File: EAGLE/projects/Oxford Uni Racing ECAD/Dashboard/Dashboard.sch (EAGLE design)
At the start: 19 parts, among them J1 T821108A1S100CEU, J2 CAN_OUT, J3 PWR_CAN, J4 DISPL, J5 BUTTONS, K1 EC2-12NU, K2 EC2-12NU, X2 D-SUB9-H2M09ST

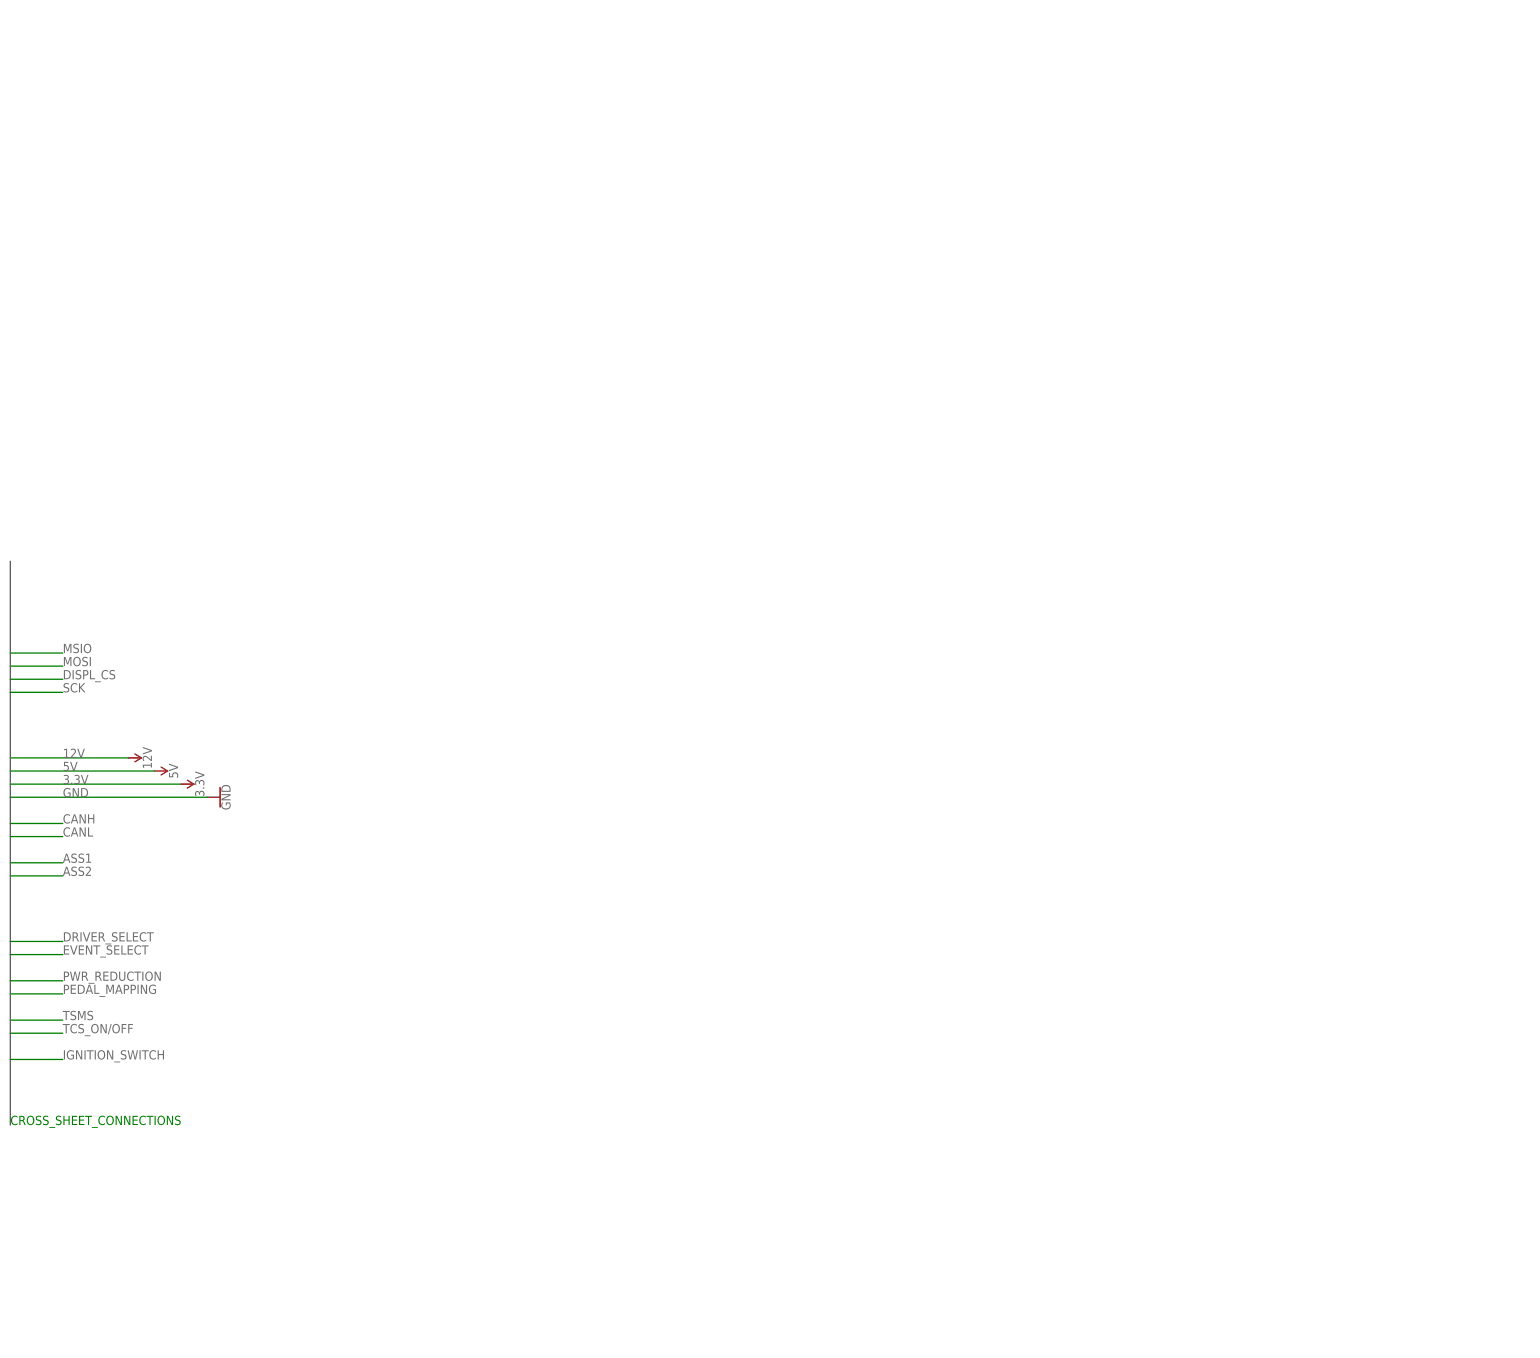
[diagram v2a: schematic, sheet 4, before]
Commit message: added microcontroller to dashboard
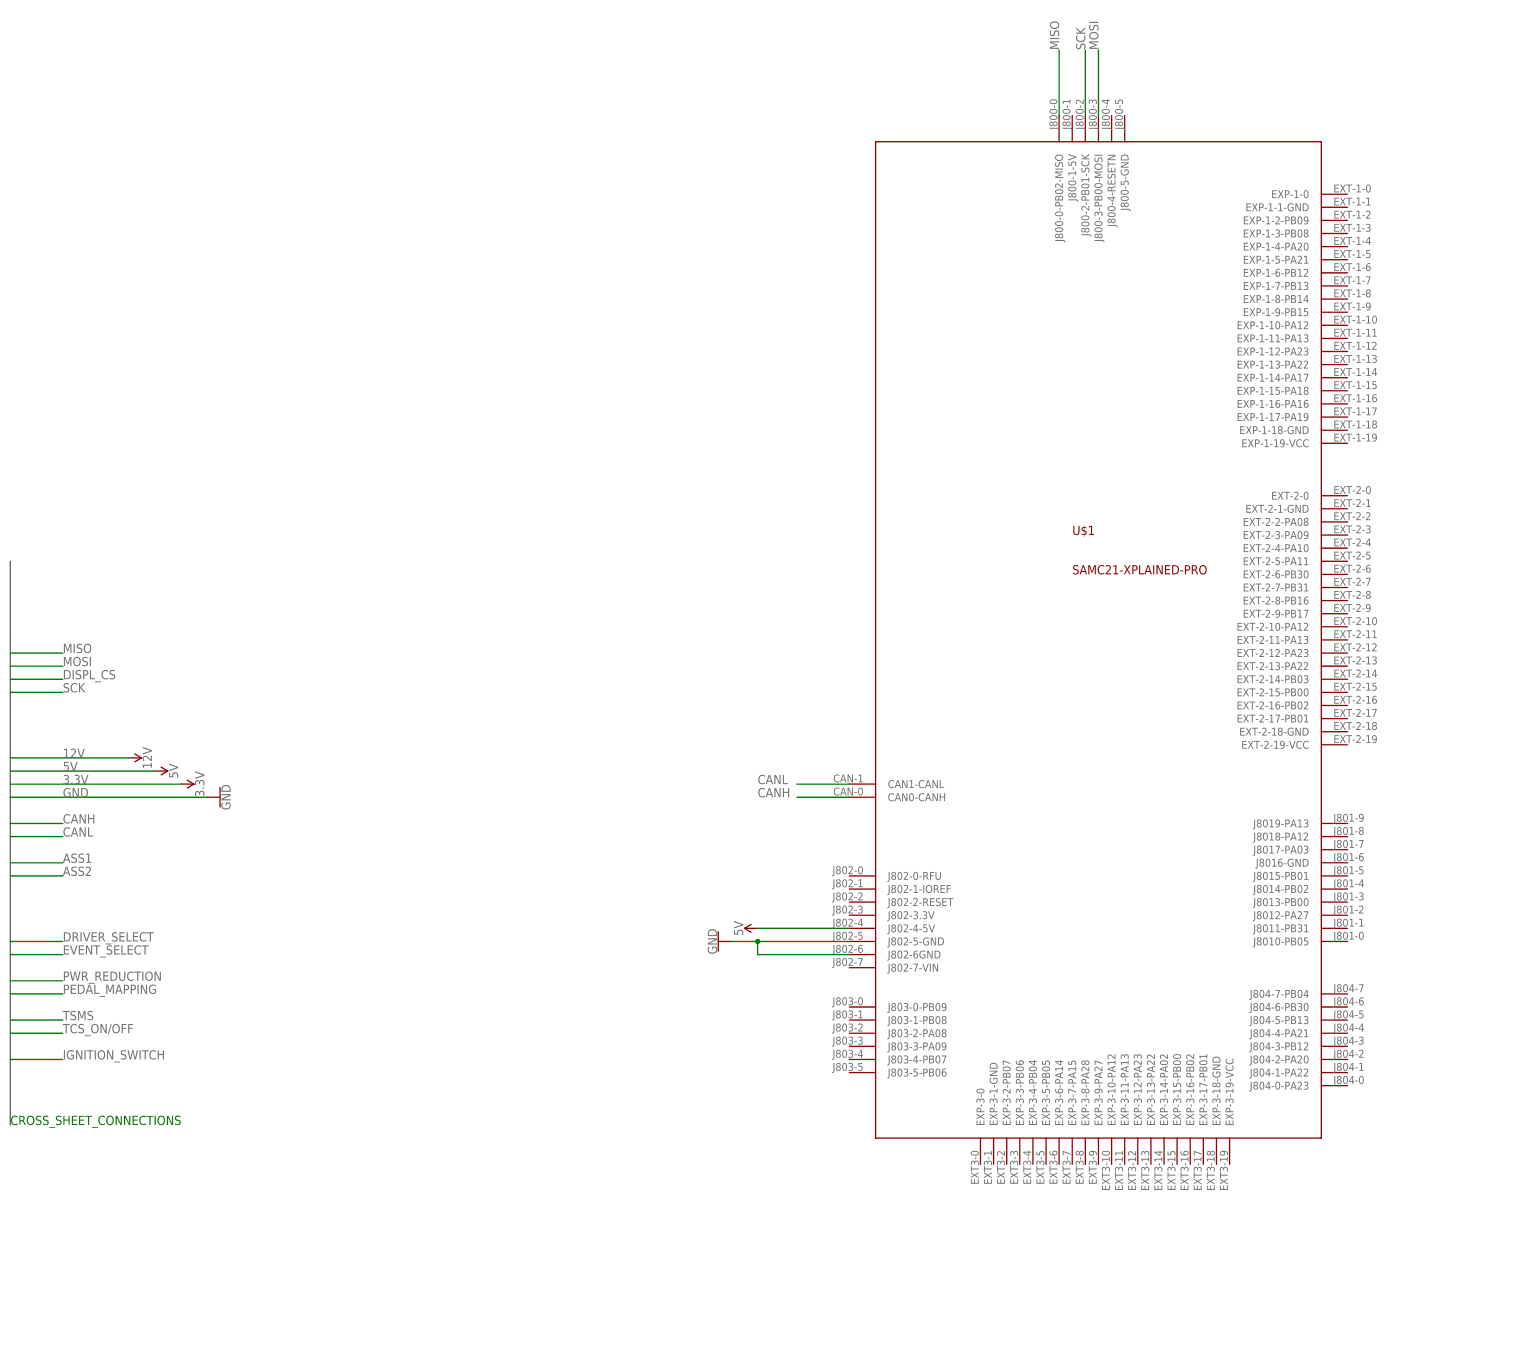
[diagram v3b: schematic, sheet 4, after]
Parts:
- added U$1: SAMC21-XPLAINED-PRO, Oxford Uni Racing Custom Blueprints:SAMC21-XPLAINED-PRO
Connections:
- removed net DISPL_SCL: J4.7
- removed net DISPL_SDA: J4.5
- new net DISPL_CS: J4.8
- new net MISO: J4.5, U$1.J800-0-PB02-MISO
- new net MOSI: J4.6, U$1.J800-3-PB00-MOSI
- new net SCK: J4.7, U$1.J800-2-PB01-SCK
- net 5V: now also U$1.J802-4-5V
- net CANH: now also U$1.CAN0-CANH
- net CANL: now also U$1.CAN1-CANL
- net GND: now also U$1.J802-5-GND, U$1.J802-6GND
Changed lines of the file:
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@@
 <part name="SUPPLY31" library="SparkFun-PowerSymbols" library_urn="urn:adsk.eagle:library:530" deviceset="3.3V" device=""/>
 <part name="GND8" library="SparkFun-PowerSymbols" library_urn="urn:adsk.eagle:library:530" deviceset="GND" device=""/>
+<part name="U$1" library="Oxford Uni Racing Custom Blueprints" deviceset="SAMC21-XPLAINED-PRO" device=""/>
+<part name="SUPPLY32" library="SparkFun-PowerSymbols" library_urn="urn:adsk.eagle:library:530" deviceset="5V" device=""/>
+<part name="GND21" library="SparkFun-PowerSymbols" library_urn="urn:adsk.eagle:library:530" deviceset="GND" device=""/>
 </parts>
 <sheets>
@@
 </segment>
 </net>
-<net name="MSIO" class="0">
+<net name="MISO" class="0">
 <segment>
 <label x="10.16" y="91.44" size="1.778" layer="95"/>
@@
 </segment>
 </net>
-<net name="MSIO" class="0">
+<net name="MISO" class="0">
 <segment>
 <label x="10.16" y="91.44" size="1.778" layer="95"/>
@@
 </segment>
 </net>
-<net name="MSIO" class="0">
+<net name="MISO" class="0">
 <segment>
 <label x="10.16" y="91.44" size="1.778" layer="95"/>
@@
 <attribute name="VALUE" x="40.894" y="63.5" size="1.778" layer="96" rot="R90" align="top-center"/>
 </instance>
+<instance part="U$1" gate="G$1" x="167.64" y="-2.54" smashed="yes">
+<attribute name="NAME" x="205.74" y="114.3" size="1.778" layer="94"/>
+<attribute name="VALUE" x="205.74" y="106.68" size="1.778" layer="94"/>
+</instance>
+<instance part="SUPPLY32" gate="G$1" x="144.78" y="38.1" smashed="yes" rot="R90">
+<attribute name="VALUE" x="141.986" y="38.1" size="1.778" layer="96" rot="R90" align="bottom-center"/>
+</instance>
+<instance part="GND21" gate="1" x="137.16" y="35.56" smashed="yes" rot="R270">
+<attribute name="VALUE" x="136.906" y="35.56" size="1.778" layer="96" rot="R270" align="top-center"/>
+</instance>
 </instances>
 <busses>
@@
 <wire x1="27.94" y1="68.58" x2="0" y2="68.58" width="0.1524" layer="91"/>
 </segment>
+<segment>
+<pinref part="U$1" gate="G$1" pin="J802-4-5V"/>
+<wire x1="162.56" y1="38.1" x2="144.78" y2="38.1" width="0.1524" layer="91"/>
+<pinref part="SUPPLY32" gate="G$1" pin="5V"/>
+</segment>
 </net>
 <net name="3.3V" class="0">
@@
 <wire x1="38.1" y1="63.5" x2="0" y2="63.5" width="0.1524" layer="91"/>
 </segment>
+<segment>
+<pinref part="U$1" gate="G$1" pin="J802-5-GND"/>
+<wire x1="162.56" y1="35.56" x2="144.78" y2="35.56" width="0.1524" layer="91"/>
+<pinref part="GND21" gate="1" pin="GND"/>
+<pinref part="U$1" gate="G$1" pin="J802-6GND"/>
+<wire x1="144.78" y1="35.56" x2="139.7" y2="35.56" width="0.1524" layer="91"/>
+<wire x1="162.56" y1="33.02" x2="144.78" y2="33.02" width="0.1524" layer="91"/>
+<wire x1="144.78" y1="33.02" x2="144.78" y2="35.56" width="0.1524" layer="91"/>
+<junction x="144.78" y="35.56"/>
+</segment>
 </net>
 <net name="CANH" class="0">
@@
 <wire x1="10.16" y1="58.42" x2="0" y2="58.42" width="0.1524" layer="91"/>
 </segment>
+<segment>
+<pinref part="U$1" gate="G$1" pin="CAN0-CANH"/>
+<wire x1="162.56" y1="63.5" x2="152.4" y2="63.5" width="0.1524" layer="91"/>
+<label x="144.78" y="63.5" size="1.778" layer="95"/>
+</segment>
 </net>
 <net name="CANL" class="0">
@@
 <wire x1="10.16" y1="55.88" x2="0" y2="55.88" width="0.1524" layer="91"/>
 </segment>
+<segment>
+<pinref part="U$1" gate="G$1" pin="CAN1-CANL"/>
+<wire x1="162.56" y1="66.04" x2="152.4" y2="66.04" width="0.1524" layer="91"/>
+<label x="144.78" y="66.04" size="1.778" layer="95"/>
+</segment>
 </net>
 <net name="ASS1" class="0">
@@
 <wire x1="10.16" y1="83.82" x2="0" y2="83.82" width="0.1524" layer="91"/>
 </segment>
+<segment>
+<pinref part="U$1" gate="G$1" pin="J800-2-PB01-SCK"/>
+<wire x1="208.28" y1="195.58" x2="208.28" y2="208.28" width="0.1524" layer="91"/>
+<label x="208.28" y="208.28" size="1.778" layer="95" rot="R90"/>
+</segment>
 </net>
 <net name="DISPL_CS" class="0">
@@
 <wire x1="10.16" y1="88.9" x2="0" y2="88.9" width="0.1524" layer="91"/>
 </segment>
-</net>
-<net name="MSIO" class="0">
+<segment>
+<pinref part="U$1" gate="G$1" pin="J800-3-PB00-MOSI"/>
+<wire x1="210.82" y1="195.58" x2="210.82" y2="208.28" width="0.1524" layer="91"/>
+<label x="210.82" y="208.28" size="1.778" layer="95" rot="R90"/>
+</segment>
+</net>
+<net name="MISO" class="0">
 <segment>
 <label x="10.16" y="91.44" size="1.778" layer="95"/>
 <wire x1="10.16" y1="91.44" x2="0" y2="91.44" width="0.1524" layer="91"/>
+</segment>
+<segment>
+<pinref part="U$1" gate="G$1" pin="J800-0-PB02-MISO"/>
+<wire x1="203.2" y1="195.58" x2="203.2" y2="208.28" width="0.1524" layer="91"/>
+<label x="203.2" y="208.28" size="1.778" layer="95" rot="R90"/>
 </segment>
 </net>
@@
 </segment>
 </net>
-<net name="MSIO" class="0">
+<net name="MISO" class="0">
 <segment>
 <label x="-50.8" y="99.06" size="1.778" layer="95"/>
@@
 </segment>
 </net>
-<net name="MSIO" class="0">
+<net name="MISO" class="0">
 <segment>
 <label x="10.16" y="91.44" size="1.778" layer="95"/>
@@
 </segment>
 </net>
-<net name="DISPL_SDA" class="0">
-<segment>
-<pinref part="J4" gate="G$1" pin="5"/>
-<wire x1="93.98" y1="50.8" x2="91.44" y2="50.8" width="0.1524" layer="91"/>
-<label x="76.2" y="50.8" size="1.778" layer="95"/>
-</segment>
-</net>
-<net name="DISPL_SCL" class="0">
-<segment>
-<pinref part="J4" gate="G$1" pin="7"/>
-<wire x1="93.98" y1="48.26" x2="91.44" y2="48.26" width="0.1524" layer="91"/>
-<label x="76.2" y="48.26" size="1.778" layer="95"/>
-</segment>
-</net>
 <net name="12V" class="0">
 <segment>
@@
 <wire x1="10.16" y1="83.82" x2="0" y2="83.82" width="0.1524" layer="91"/>
 </segment>
+<segment>
+<pinref part="J4" gate="G$1" pin="7"/>
+<wire x1="93.98" y1="48.26" x2="91.44" y2="48.26" width="0.1524" layer="91"/>
+<label x="83.82" y="48.26" size="1.778" layer="95"/>
+</segment>
 </net>
 <net name="DISPL_CS" class="0">
@@
 <wire x1="10.16" y1="86.36" x2="0" y2="86.36" width="0.1524" layer="91"/>
 </segment>
+<segment>
+<pinref part="J4" gate="G$1" pin="8"/>
+<wire x1="114.3" y1="48.26" x2="116.84" y2="48.26" width="0.1524" layer="91"/>
+<label x="116.84" y="48.26" size="1.778" layer="95"/>
+</segment>
 </net>
 <net name="MOSI" class="0">
@@
 <wire x1="10.16" y1="88.9" x2="0" y2="88.9" width="0.1524" layer="91"/>
 </segment>
-</net>
-<net name="MSIO" class="0">
+<segment>
+<pinref part="J4" gate="G$1" pin="6"/>
+<wire x1="114.3" y1="50.8" x2="116.84" y2="50.8" width="0.1524" layer="91"/>
+<label x="116.84" y="50.8" size="1.778" layer="95"/>
+</segment>
+</net>
+<net name="MISO" class="0">
 <segment>
 <label x="10.16" y="91.44" size="1.778" layer="95"/>
 <wire x1="10.16" y1="91.44" x2="0" y2="91.44" width="0.1524" layer="91"/>
+</segment>
+<segment>
+<pinref part="J4" gate="G$1" pin="5"/>
+<wire x1="93.98" y1="50.8" x2="91.44" y2="50.8" width="0.1524" layer="91"/>
+<label x="83.82" y="50.8" size="1.778" layer="95"/>
 </segment>
 </net>
@@
 </segment>
 </net>
-<net name="MSIO" class="0">
+<net name="MISO" class="0">
 <segment>
 <label x="10.16" y="91.44" size="1.778" layer="95"/>

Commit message: connected buttons to digital IO pins
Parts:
- removed J5: BUTTONS, T821108A1S100CEU:T821108A1S100CEU
- added J6, J7: BUTTONS, T821108A1S100CEU:T821108A1S100CEU
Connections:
- removed net BRAKE_BIAS: J5.6
- removed net DRIVER_SELECT: J5.1
- removed net EMERGENCY_STOP: J5.7
- removed net EVENT_SELECT: J5.3
- removed net PEDAL_MAPPING: J5.4
- new net DRIVER_SELECT_1: J7.1, U$1.J804-6-PB30
- new net DRIVER_SELECT_2: J7.3, U$1.J804-5-PB13
- new net DRIVER_SELECT_3: J7.5, U$1.J804-4-PA21
- new net DRIVER_SELECT_4: J7.7, U$1.J804-3-PB12
- new net DRIVER_SELECT_5: J7.8, U$1.J804-2-PA20
- new net EVENT_SELECT_1: J6.1, U$1.EXP-3-5-PB05
- new net EVENT_SELECT_2: J6.3, U$1.EXP-3-4-PB04
- new net EVENT_SELECT_3: J6.5, U$1.EXP-3-3-PB06
- new net EVENT_SELECT_4: J6.7, U$1.EXP-3-2-PB07
- new net PEDAL_MAPPING_1: J7.6, U$1.J8011-PB31
- new net PEDAL_MAPPING_2: J7.4, U$1.J8010-PB05
- net 5V: now also J6.2, J7.2
- net DISPL_CS: now also U$1.J804-7-PB04
- net IGNITION_SWITCH: now also J6.8, U$1.EXP-3-14-PA02; no longer J5.5
- net PWR_REDUCTION: now also J6.4, U$1.EXP-3-9-PA27; no longer J5.2
- net TCS_ON/OFF: now also J6.6, U$1.EXP-3-8-PA28; no longer J5.8
